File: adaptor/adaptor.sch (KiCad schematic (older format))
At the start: 12 parts, among them J1 RJ45, J2 RJ45, K1 DC Jack, K2 GPIO, P2 nRF24l01, P3 ISP, P6 Clock, P7 Out, P8 In, P9 Serial

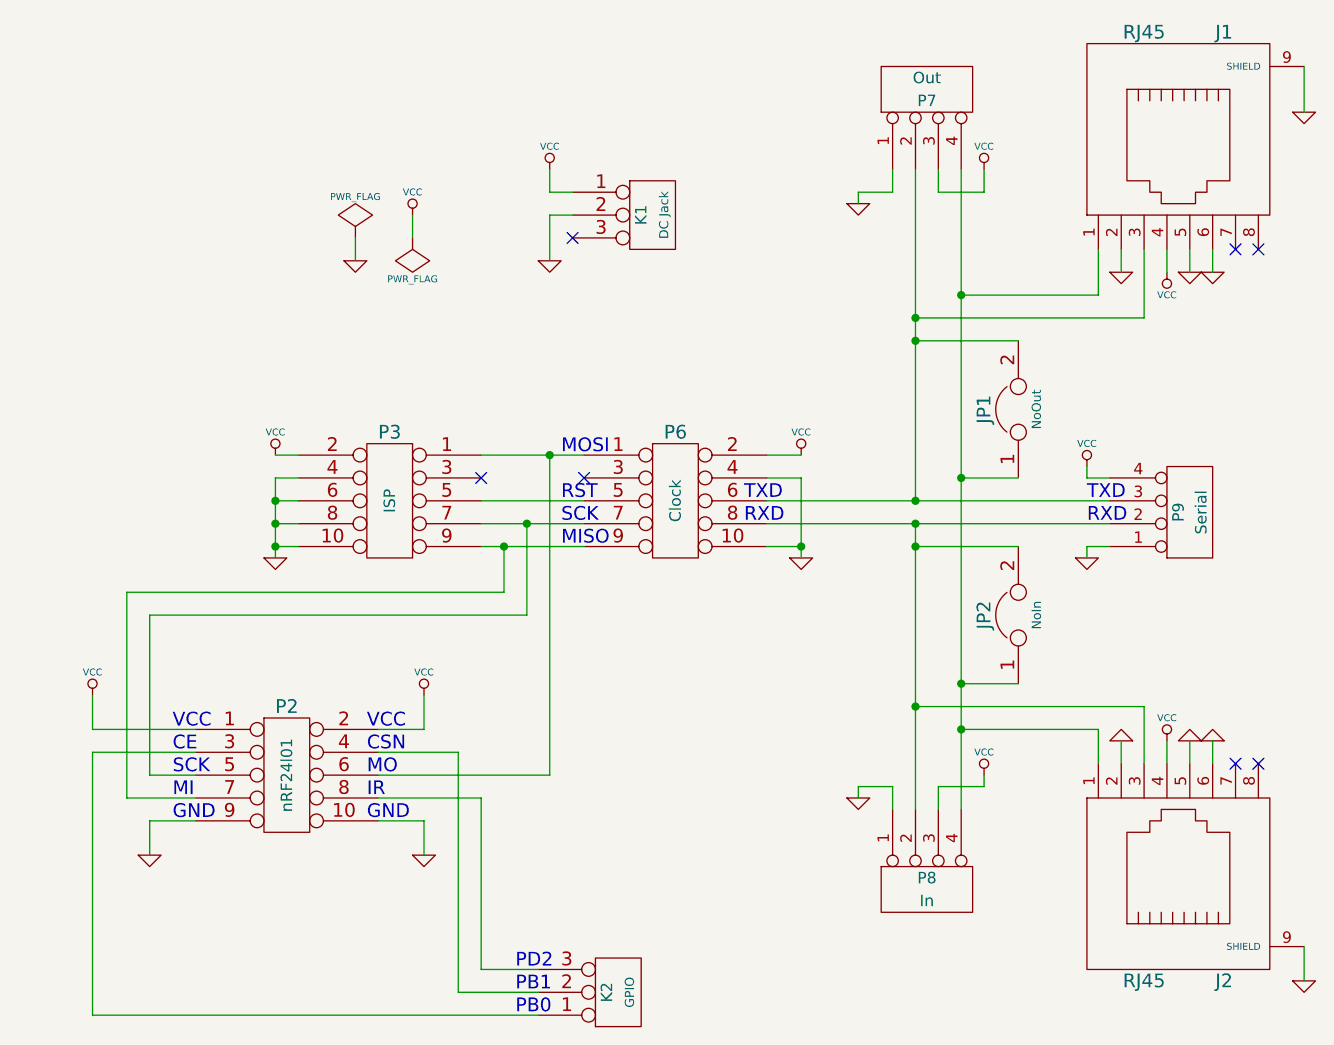
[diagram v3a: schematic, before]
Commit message: Add descriptive net names
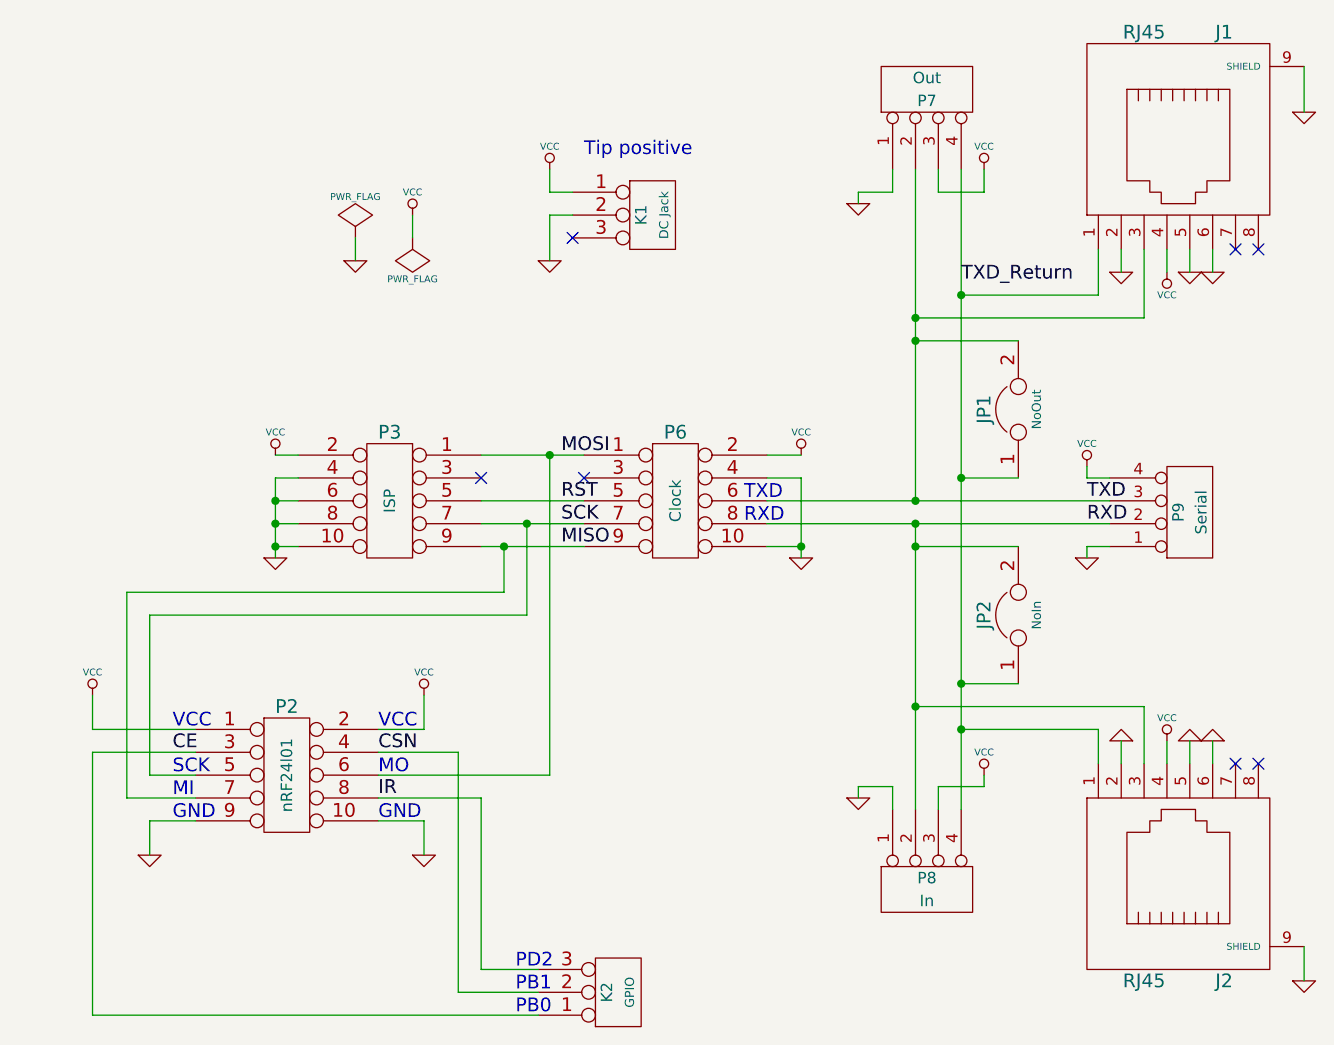
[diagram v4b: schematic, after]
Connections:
- net MOSI: now reaches P2.6, P3.1, P6.1
- net RST: now reaches P3.5, P6.5
- net TXD: now reaches J1.3, JP1.2, P6.6, P7.2 (P2), P9.3 (P3)
- net SCK: now reaches P2.5, P3.7, P6.7
- net RXD: now reaches J2.3, JP2.2, P6.8, P8.2 (P2), P9.2 (P2)
- net MISO: now reaches P2.7, P3.9, P6.9
- net CE: now reaches K2.1 (P1), P2.3
- net CSN: now reaches K2.2 (PM), P2.4
- net IR: now reaches K2.3 (P3), P2.8
- net TXD_Return: now reaches J1.1, J2.1, JP1.1, JP2.1, P7.4 (P4), P8.4 (P4)
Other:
- note added: "Tip positive"
- note removed: "CE"
- note removed: "CSN"
- note removed: "IR"
- note removed: "MISO"
- note removed: "MOSI"
- note removed: "RST"
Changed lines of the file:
@@
-EESchema Schematic File Version 2  date Mon 11 Feb 2013 12:07:26 EST
+EESchema Schematic File Version 2  date Mon 11 Feb 2013 12:27:24 EST
 LIBS:power
 LIBS:device
@@
 Comment4 ""
 $EndDescr
+Text Notes 3650 2100 0    60   ~ 0
+Tip positive
+Text Label 1850 4700 0    60   ~ 0
+CE
+Text Label 2750 4900 0    60   ~ 0
+IR
+Text Label 2750 4700 0    60   ~ 0
+CSN
+Text Label 3550 3800 0    60   ~ 0
+MISO
+Text Label 3550 3700 0    60   ~ 0
+SCK
+Text Label 3550 3600 0    60   ~ 0
+RST
+Text Label 3550 3400 0    60   ~ 0
+MOSI
+Text Label 5300 2650 0    60   ~ 0
+TXD_Return
+Text Label 5850 3700 0    60   ~ 0
+RXD
+Text Label 5850 3600 0    60   ~ 0
+TXD
 Wire Wire Line
 	3450 5650 3200 5650
@@
 NoConn ~ 3600 2450
 $Comp
-L GND #PWR10
+L GND #PWR01
 U 1 1 50F1333C
 P 3500 2550
-F 0 "#PWR10" H 3500 2550 30  0001 C CNN
+F 0 "#PWR01" H 3500 2550 30  0001 C CNN
 F 1 "GND" H 3500 2480 30  0001 C CNN
 	1    3500 2550
@@
 $EndComp
 $Comp
-L VCC #PWR9
+L VCC #PWR02
 U 1 1 50F1333A
 P 3500 2150
-F 0 "#PWR9" H 3500 2250 30  0001 C CNN
+F 0 "#PWR02" H 3500 2250 30  0001 C CNN
 F 1 "VCC" H 3500 2250 30  0000 C CNN
 	1    3500 2150
@@
 $EndComp
 $Comp
-L GND #PWR28
+L GND #PWR03
 U 1 1 50F12E86
 P 6800 5700
-F 0 "#PWR28" H 6800 5700 30  0001 C CNN
+F 0 "#PWR03" H 6800 5700 30  0001 C CNN
 F 1 "GND" H 6800 5630 30  0001 C CNN
 	1    6800 5700
@@
 $EndComp
 $Comp
-L GND #PWR27
+L GND #PWR04
 U 1 1 50F12E82
 P 6800 1900
-F 0 "#PWR27" H 6800 1900 30  0001 C CNN
+F 0 "#PWR04" H 6800 1900 30  0001 C CNN
 F 1 "GND" H 6800 1830 30  0001 C CNN
 	1    6800 1900
@@
 NoConn ~ 6500 4750
 $Comp
-L VCC #PWR22
+L VCC #PWR05
 U 1 1 50F12CA2
 P 6200 4650
-F 0 "#PWR22" H 6200 4750 30  0001 C CNN
+F 0 "#PWR05" H 6200 4750 30  0001 C CNN
 F 1 "VCC" H 6200 4750 30  0000 C CNN
 	1    6200 4650
@@
 $EndComp
 $Comp
-L GND #PWR20
+L GND #PWR06
 U 1 1 50F12C9D
 P 6000 4650
-F 0 "#PWR20" H 6000 4650 30  0001 C CNN
+F 0 "#PWR06" H 6000 4650 30  0001 C CNN
 F 1 "GND" H 6000 4580 30  0001 C CNN
 	1    6000 4650
@@
 $EndComp
 $Comp
-L GND #PWR24
+L GND #PWR07
 U 1 1 50F12C9B
 P 6300 4650
-F 0 "#PWR24" H 6300 4650 30  0001 C CNN
+F 0 "#PWR07" H 6300 4650 30  0001 C CNN
 F 1 "GND" H 6300 4580 30  0001 C CNN
 	1    6300 4650
@@
 $EndComp
 $Comp
-L GND #PWR26
+L GND #PWR08
 U 1 1 50F12C91
 P 6400 4650
-F 0 "#PWR26" H 6400 4650 30  0001 C CNN
+F 0 "#PWR08" H 6400 4650 30  0001 C CNN
 F 1 "GND" H 6400 4580 30  0001 C CNN
 	1    6400 4650
@@
 NoConn ~ 6500 2500
 $Comp
-L GND #PWR23
+L GND #PWR09
 U 1 1 50F12C36
 P 6300 2600
-F 0 "#PWR23" H 6300 2600 30  0001 C CNN
+F 0 "#PWR09" H 6300 2600 30  0001 C CNN
 F 1 "GND" H 6300 2530 30  0001 C CNN
 	1    6300 2600
@@
 $EndComp
 $Comp
-L VCC #PWR21
+L VCC #PWR010
 U 1 1 50F12C0E
 P 6200 2600
-F 0 "#PWR21" H 6200 2700 30  0001 C CNN
+F 0 "#PWR010" H 6200 2700 30  0001 C CNN
 F 1 "VCC" H 6200 2700 30  0000 C CNN
 	1    6200 2600
@@
 $EndComp
 $Comp
-L GND #PWR25
+L GND #PWR011
 U 1 1 50F12BB0
 P 6400 2600
-F 0 "#PWR25" H 6400 2600 30  0001 C CNN
+F 0 "#PWR011" H 6400 2600 30  0001 C CNN
 F 1 "GND" H 6400 2530 30  0001 C CNN
 	1    6400 2600
@@
 $EndComp
 $Comp
-L GND #PWR19
+L GND #PWR012
 U 1 1 50F12BAE
 P 6000 2600
-F 0 "#PWR19" H 6000 2600 30  0001 C CNN
+F 0 "#PWR012" H 6000 2600 30  0001 C CNN
 F 1 "GND" H 6000 2530 30  0001 C CNN
 	1    6000 2600
@@
 $EndComp
 $Comp
-L PWR_FLAG #FLG2
+L PWR_FLAG #FLG013
 U 1 1 50F108B5
 P 2900 2450
-F 0 "#FLG2" H 2900 2545 30  0001 C CNN
+F 0 "#FLG013" H 2900 2545 30  0001 C CNN
 F 1 "PWR_FLAG" H 2900 2630 30  0000 C CNN
 	1    2900 2450
@@
 $EndComp
 $Comp
-L PWR_FLAG #FLG1
+L PWR_FLAG #FLG014
 U 1 1 50F108AE
 P 2650 2450
-F 0 "#FLG1" H 2650 2545 30  0001 C CNN
+F 0 "#FLG014" H 2650 2545 30  0001 C CNN
 F 1 "PWR_FLAG" H 2650 2630 30  0000 C CNN
 	1    2650 2450
@@
 $EndComp
 $Comp
-L VCC #PWR6
+L VCC #PWR015
 U 1 1 50F10847
 P 2900 2350
-F 0 "#PWR6" H 2900 2450 30  0001 C CNN
+F 0 "#PWR015" H 2900 2450 30  0001 C CNN
 F 1 "VCC" H 2900 2450 30  0000 C CNN
 	1    2900 2350
@@
 $EndComp
 $Comp
-L GND #PWR5
+L GND #PWR016
 U 1 1 50F10843
 P 2650 2550
-F 0 "#PWR5" H 2650 2550 30  0001 C CNN
+F 0 "#PWR016" H 2650 2550 30  0001 C CNN
 F 1 "GND" H 2650 2480 30  0001 C CNN
 	1    2650 2550
@@
 PB0
 $Comp
-L VCC #PWR7
+L VCC #PWR017
 U 1 1 50F1045B
 P 2950 4450
-F 0 "#PWR7" H 2950 4550 30  0001 C CNN
+F 0 "#PWR017" H 2950 4550 30  0001 C CNN
 F 1 "VCC" H 2950 4550 30  0000 C CNN
 	1    2950 4450
@@
 $EndComp
 $Comp
-L VCC #PWR1
+L VCC #PWR018
 U 1 1 50F10458
 P 1500 4450
-F 0 "#PWR1" H 1500 4550 30  0001 C CNN
+F 0 "#PWR018" H 1500 4550 30  0001 C CNN
 F 1 "VCC" H 1500 4550 30  0000 C CNN
 	1    1500 4450
@@
 $EndComp
 $Comp
-L GND #PWR2
+L GND #PWR019
 U 1 1 50F10445
 P 1750 5150
-F 0 "#PWR2" H 1750 5150 30  0001 C CNN
+F 0 "#PWR019" H 1750 5150 30  0001 C CNN
 F 1 "GND" H 1750 5080 30  0001 C CNN
 	1    1750 5150
@@
 $EndComp
 $Comp
-L GND #PWR8
+L GND #PWR020
 U 1 1 50F10444
 P 2950 5150
-F 0 "#PWR8" H 2950 5150 30  0001 C CNN
+F 0 "#PWR020" H 2950 5150 30  0001 C CNN
 F 1 "GND" H 2950 5080 30  0001 C CNN
 	1    2950 5150
 	1    0    0    -1
 $EndComp
-Text Notes 1850 4700 0    60   ~ 0
-CE
-Text Notes 2700 4700 0    60   ~ 0
-CSN
 Text Notes 1850 4800 0    60   ~ 0
 SCK
-Text Notes 2700 4800 0    60   ~ 0
+Text Notes 2750 4800 0    60   ~ 0
 MO
-Text Notes 2700 4900 0    60   ~ 0
-IR
 Text Notes 1850 4900 0    60   ~ 0
 MI
-Text Notes 2700 5000 0    60   ~ 0
+Text Notes 2750 5000 0    60   ~ 0
 GND
 Text Notes 1850 5000 0    60   ~ 0
@@
 Text Notes 1850 4600 0    60   ~ 0
 VCC
-Text Notes 2700 4600 0    60   ~ 0
+Text Notes 2750 4600 0    60   ~ 0
 VCC
 $Comp
-L VCC #PWR16
+L VCC #PWR021
 U 1 1 50F0FB10
 P 5400 4800
-F 0 "#PWR16" H 5400 4900 30  0001 C CNN
+F 0 "#PWR021" H 5400 4900 30  0001 C CNN
 F 1 "VCC" H 5400 4900 30  0000 C CNN
 	1    5400 4800
@@
 $EndComp
 $Comp
-L VCC #PWR15
+L VCC #PWR022
 U 1 1 50F0FB0C
 P 5400 2150
-F 0 "#PWR15" H 5400 2250 30  0001 C CNN
+F 0 "#PWR022" H 5400 2250 30  0001 C CNN
 F 1 "VCC" H 5400 2250 30  0000 C CNN
 	1    5400 2150
 	1    0    0    -1
 $EndComp
-Text Notes 5850 3700 0    60   ~ 0
-RXD
-Text Notes 5850 3600 0    60   ~ 0
-TXD
-Text Notes 3550 3800 0    60   ~ 0
-MISO
-Text Notes 3550 3700 0    60   ~ 0
-SCK
-Text Notes 3550 3600 0    60   ~ 0
-RST
-Text Notes 3550 3400 0    60   ~ 0
-MOSI
 Text Notes 4350 3700 0    60   ~ 0
 RXD
@@
 TXD
 $Comp
-L VCC #PWR17
+L VCC #PWR023
 U 1 1 50F0FA0F
 P 5850 3450
-F 0 "#PWR17" H 5850 3550 30  0001 C CNN
+F 0 "#PWR023" H 5850 3550 30  0001 C CNN
 F 1 "VCC" H 5850 3550 30  0000 C CNN
 	1    5850 3450
@@
 $EndComp
 $Comp
-L GND #PWR18
+L GND #PWR024
 U 1 1 50F0F963
 P 5850 3850
-F 0 "#PWR18" H 5850 3850 30  0001 C CNN
+F 0 "#PWR024" H 5850 3850 30  0001 C CNN
 F 1 "GND" H 5850 3780 30  0001 C CNN
 	1    5850 3850
@@
 $EndComp
 $Comp
-L GND #PWR13
+L GND #PWR025
 U 1 1 50F0F960
 P 4850 2300
-F 0 "#PWR13" H 4850 2300 30  0001 C CNN
+F 0 "#PWR025" H 4850 2300 30  0001 C CNN
 F 1 "GND" H 4850 2230 30  0001 C CNN
 	1    4850 2300
@@
 $EndComp
 $Comp
-L GND #PWR14
+L GND #PWR026
 U 1 1 50F0F95D
 P 4850 4900
-F 0 "#PWR14" H 4850 4900 30  0001 C CNN
+F 0 "#PWR026" H 4850 4900 30  0001 C CNN
 F 1 "GND" H 4850 4830 30  0001 C CNN
 	1    4850 4900
@@
 $EndComp
 $Comp
-L GND #PWR4
+L GND #PWR027
 U 1 1 50F0F7F8
 P 2300 3850
-F 0 "#PWR4" H 2300 3850 30  0001 C CNN
+F 0 "#PWR027" H 2300 3850 30  0001 C CNN
 F 1 "GND" H 2300 3780 30  0001 C CNN
 	1    2300 3850
@@
 $EndComp
 $Comp
-L VCC #PWR3
+L VCC #PWR028
 U 1 1 50F0F7F5
 P 2300 3400
-F 0 "#PWR3" H 2300 3500 30  0001 C CNN
+F 0 "#PWR028" H 2300 3500 30  0001 C CNN
 F 1 "VCC" H 2300 3500 30  0000 C CNN
 	1    2300 3400
@@
 NoConn ~ 3650 3500
 $Comp
-L GND #PWR12
+L GND #PWR029
 U 1 1 50F0F787
 P 4600 3850
-F 0 "#PWR12" H 4600 3850 30  0001 C CNN
+F 0 "#PWR029" H 4600 3850 30  0001 C CNN
 F 1 "GND" H 4600 3780 30  0001 C CNN
 	1    4600 3850
@@
 $EndComp
 $Comp
-L VCC #PWR11
+L VCC #PWR030
 U 1 1 50F0F780
 P 4600 3400
-F 0 "#PWR11" H 4600 3500 30  0001 C CNN
+F 0 "#PWR030" H 4600 3500 30  0001 C CNN
 F 1 "VCC" H 4600 3500 30  0000 C CNN
 	1    4600 3400
